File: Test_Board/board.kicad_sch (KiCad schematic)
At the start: 58 parts, among them J1 conn, J2 Conn_01x06, J3 ST-link, SW1 reset, U1 AZ1117-3.3, U2 ICM-42688-P, U3 QMC5883P, U4 BMI270, U5 BMP388, U6 STM32F103C8Tx

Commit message: This commits updates BOM for Test Board, Changes the Ferrit bead value
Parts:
- C1: JLCPCB PART# (none) -> C19702
- C10, C13, C14, C16, C18, C2, C20, C5, C8, C9: JLCPCB PART# (none) -> C14663
- C11, C17: JLCPCB PART# (none) -> C15849
- C12, C4: JLCPCB PART# (none) -> C1705
- C15: value 100n -> 0.1uF; JLCPCB PART# (none) -> C14663
- C19, C7: JLCPCB PART# (none) -> C100042
- C3: JLCPCB PART# (none) -> C86295
- C6: JLCPCB PART# (none) -> C23630
- D1, D2, D3, D4: JLCPCB PART# (none) -> C20608785
- FB1: value 120r @ 100KHz -> 1k@100Mhz; JLCPCB PART# (none) -> C44838
- R1: JLCPCB PART# (none) -> C95177
- R10: JLCPCB PART# (none) -> C98220
- R11, R12: JLCPCB PART# (none) -> C107701
- R13: footprint Resistor_SMD:R_0402_1005Metric -> Resistor_SMD:R_0603_1608Metric; JLCPCB PART# (none) -> C98220
- R2, R3, R8, R9: JLCPCB PART# (none) -> C2904521
- R4, R5, R6, R7: JLCPCB PART# (none) -> C105881
- SW1: JLCPCB PART# (none) -> C115357
- U1: JLCPCB PART# (none) -> C108495
- U4: JLCPCB PART# (none) -> C2836813
- U5: JLCPCB PART# (none) -> C779278
- U6: JLCPCB PART# (none) -> C8734

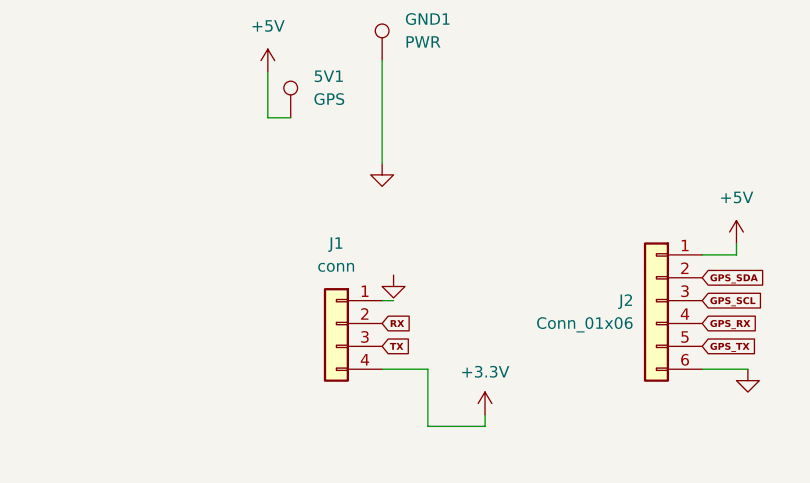
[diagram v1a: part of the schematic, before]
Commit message: added quatronion filter, CRSF protocol, and PID loops
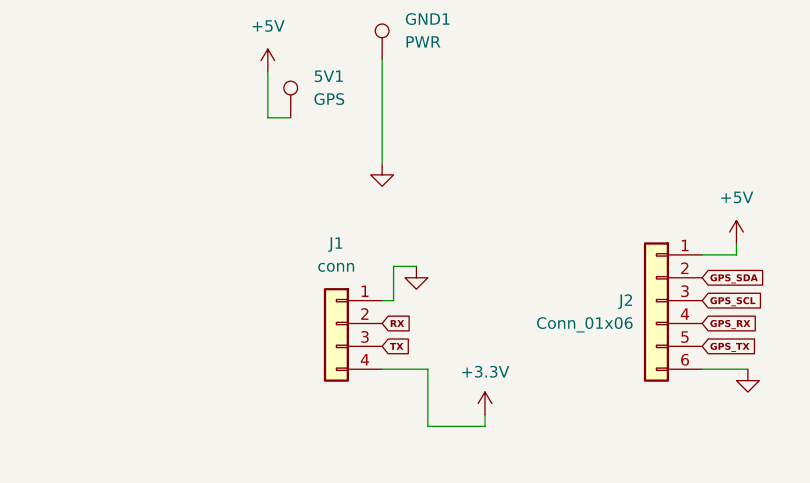
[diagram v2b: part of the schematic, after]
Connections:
- net GND: now also J1.1 (Pin_1)
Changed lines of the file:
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@@
 	(wire
 		(pts
-			(xy 53.34 265.43) (xy 52.07 265.43)
+			(xy 55.88 261.62) (xy 53.34 261.62)
 		)
 		(stroke
@@
 	(wire
 		(pts
+			(xy 53.34 261.62) (xy 53.34 265.43)
+		)
+		(stroke
+			(width 0)
+			(type default)
+		)
+	)
+	(wire
+		(pts
 			(xy 81.28 129.54) (xy 81.28 127)
 		)
@@
 	(wire
 		(pts
+			(xy 53.34 265.43) (xy 52.07 265.43)
+		)
+		(stroke
+			(width 0)
+			(type default)
+		)
+	)
+	(wire
+		(pts
 			(xy 90.17 170.18) (xy 90.17 172.72)
 		)
@@
 	(symbol
 		(lib_id "power:GND")
-		(at 53.34 262.588 0)
+		(at 55.88 261.62 0)
 		(unit 1)
 		(exclude_from_sim no)
@@
 		(fields_autoplaced yes)
 		(property "Reference" "#PWR011"
-			(at 53.34 268.938 0)
+			(at 55.88 267.97 0)
 			(effects
 				(font
@@
 		)
 		(property "Value" "GND"
-			(at 53.34 267.668 0)
+			(at 55.88 266.7 0)
 			(effects
 				(font
@@
 		)
 		(property "Footprint" ""
-			(at 53.34 262.588 0)
+			(at 55.88 261.62 0)
 			(effects
 				(font
@@
 		)
 		(property "Datasheet" ""
-			(at 53.34 262.588 0)
+			(at 55.88 261.62 0)
 			(effects
 				(font
@@
 		)
 		(property "Description" "Power symbol creates a global label with name \"GND\" , ground"
-			(at 53.34 262.588 0)
+			(at 55.88 261.62 0)
 			(effects
 				(font
